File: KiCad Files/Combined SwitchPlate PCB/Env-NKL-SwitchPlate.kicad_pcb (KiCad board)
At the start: 2 copper layers, 366.6 x 119.2 mm, 8 parts

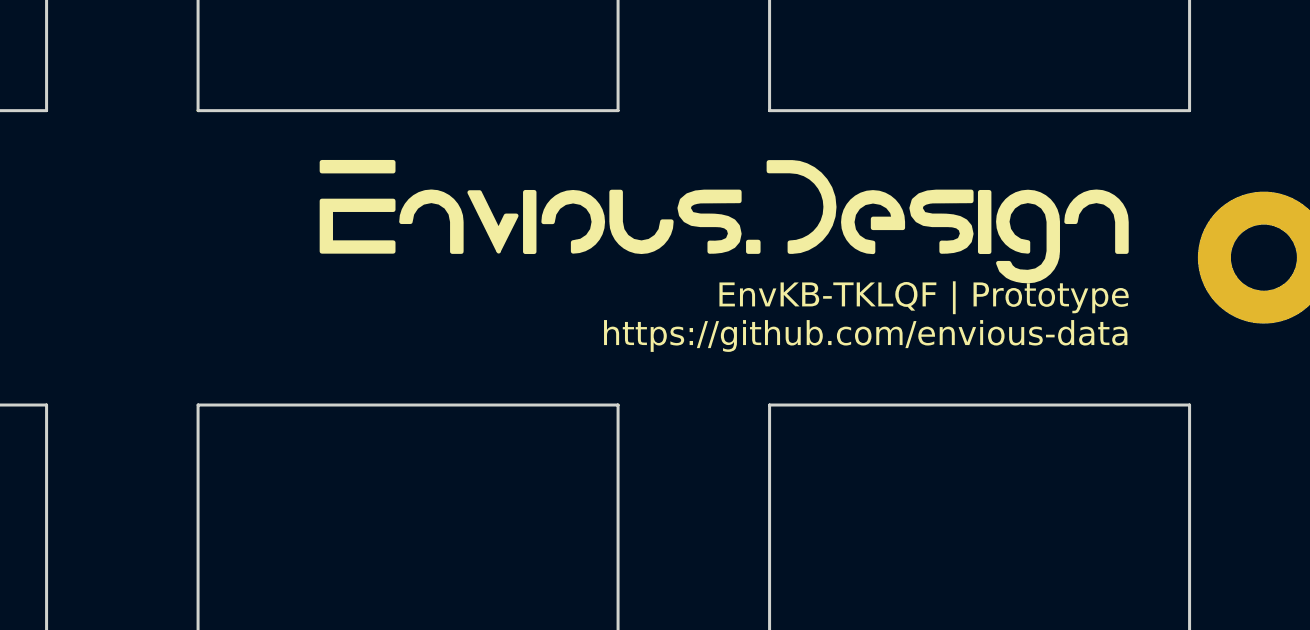
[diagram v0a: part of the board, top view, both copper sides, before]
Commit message: checked alignment and updated incorrect silkscreen.
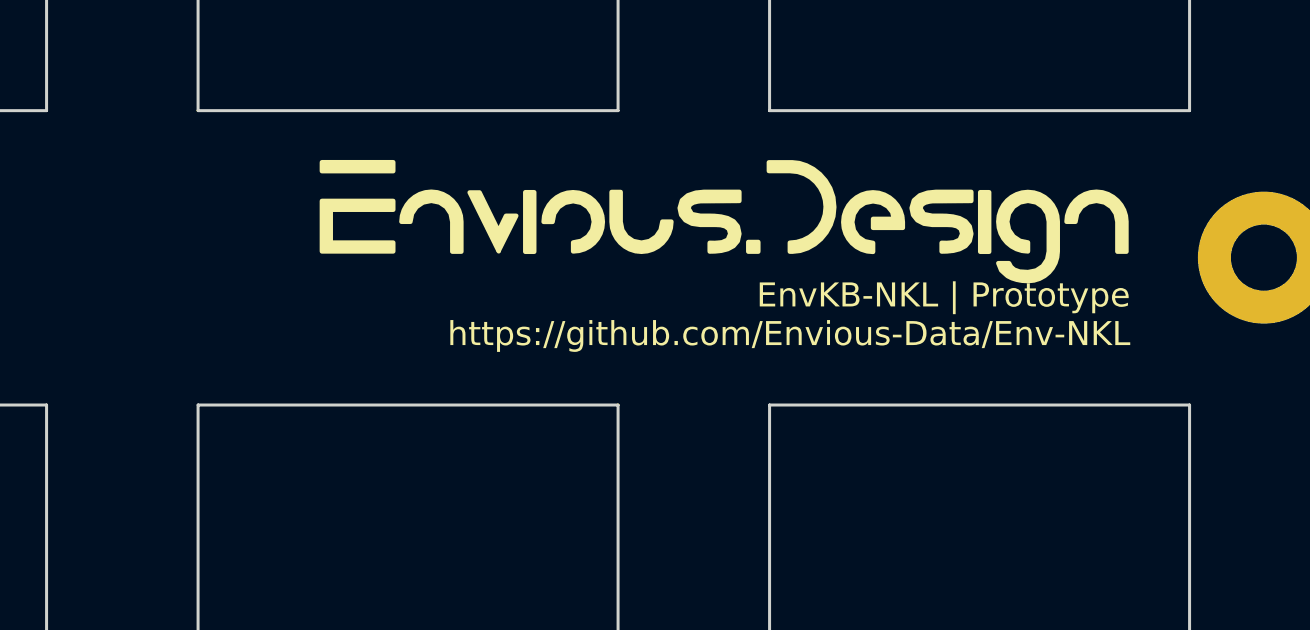
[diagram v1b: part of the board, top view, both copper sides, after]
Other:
- board text added: "EnvKB-NKL | Prototype https://github.com/Envious-Data/Env-NKL"
- board text removed: "EnvKB-TKLQF | Prototype https://github.com/envious-data"
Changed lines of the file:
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@@
 		(layer "Edge.Cuts")
 	)
-	(gr_text "EnvKB-TKLQF | Prototype\nhttps://github.com/envious-data"
+	(gr_text "EnvKB-NKL | Prototype\nhttps://github.com/Envious-Data/Env-NKL"
 		(at 392.75 58.3 0)
 		(layer "F.SilkS")
